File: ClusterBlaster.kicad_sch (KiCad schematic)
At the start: 12 parts, among them J1 Conn_01x04, U1 LM339, U2 L7805

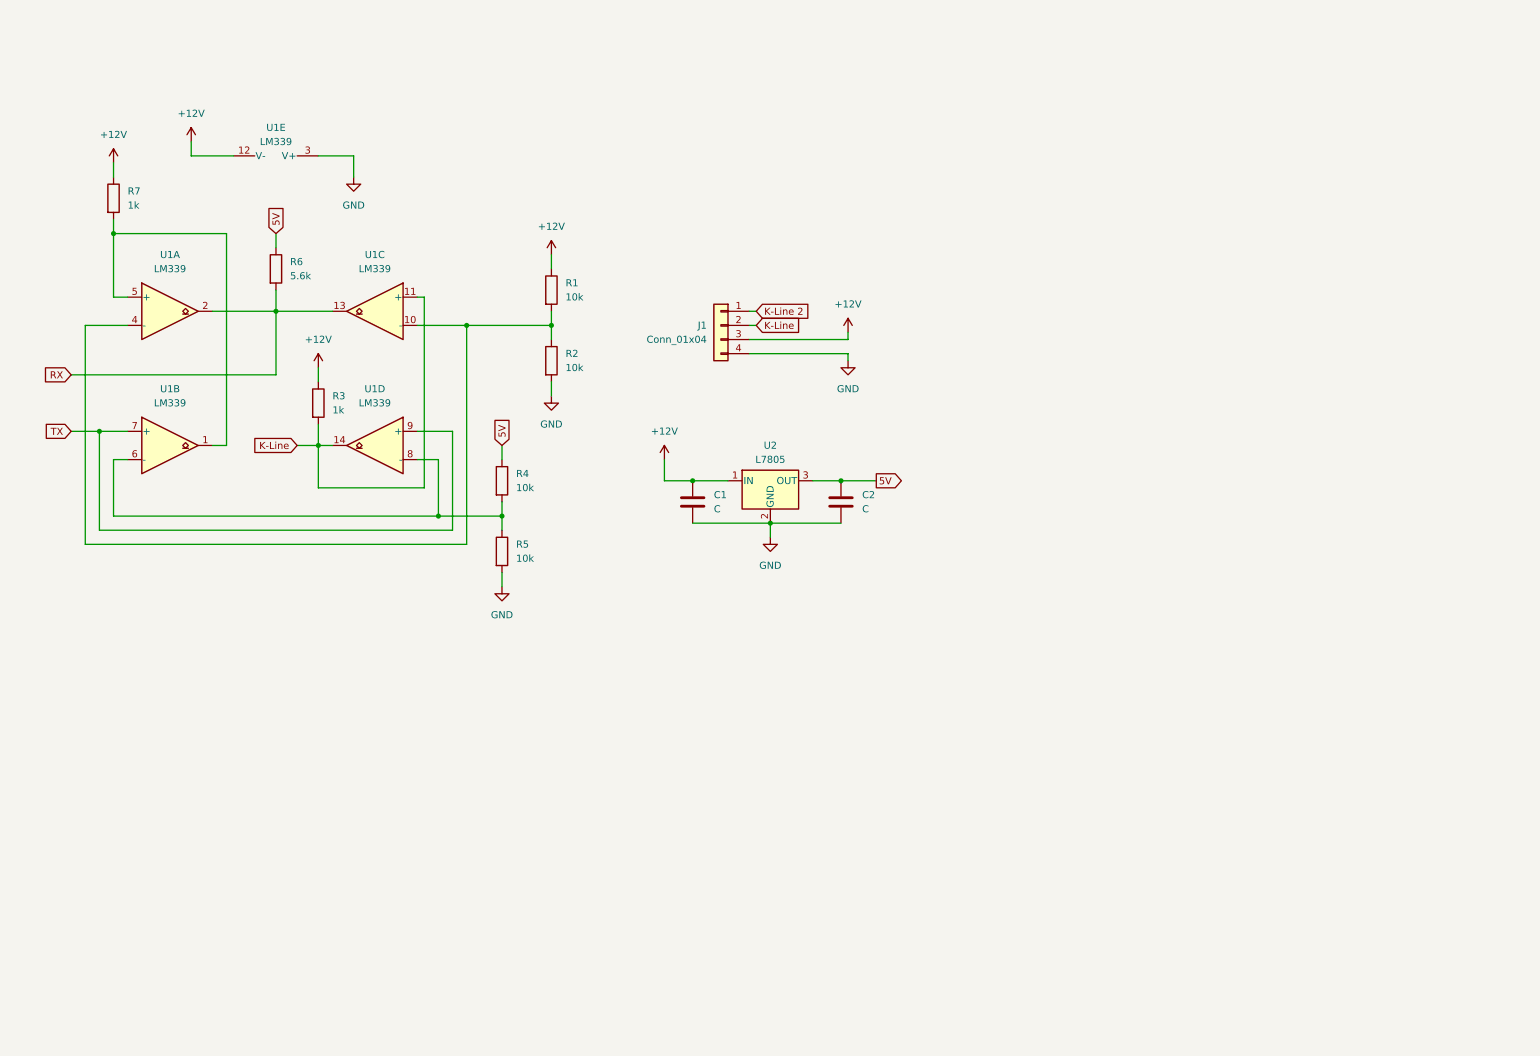
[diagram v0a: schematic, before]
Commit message: Added Arduino symbol and footprint
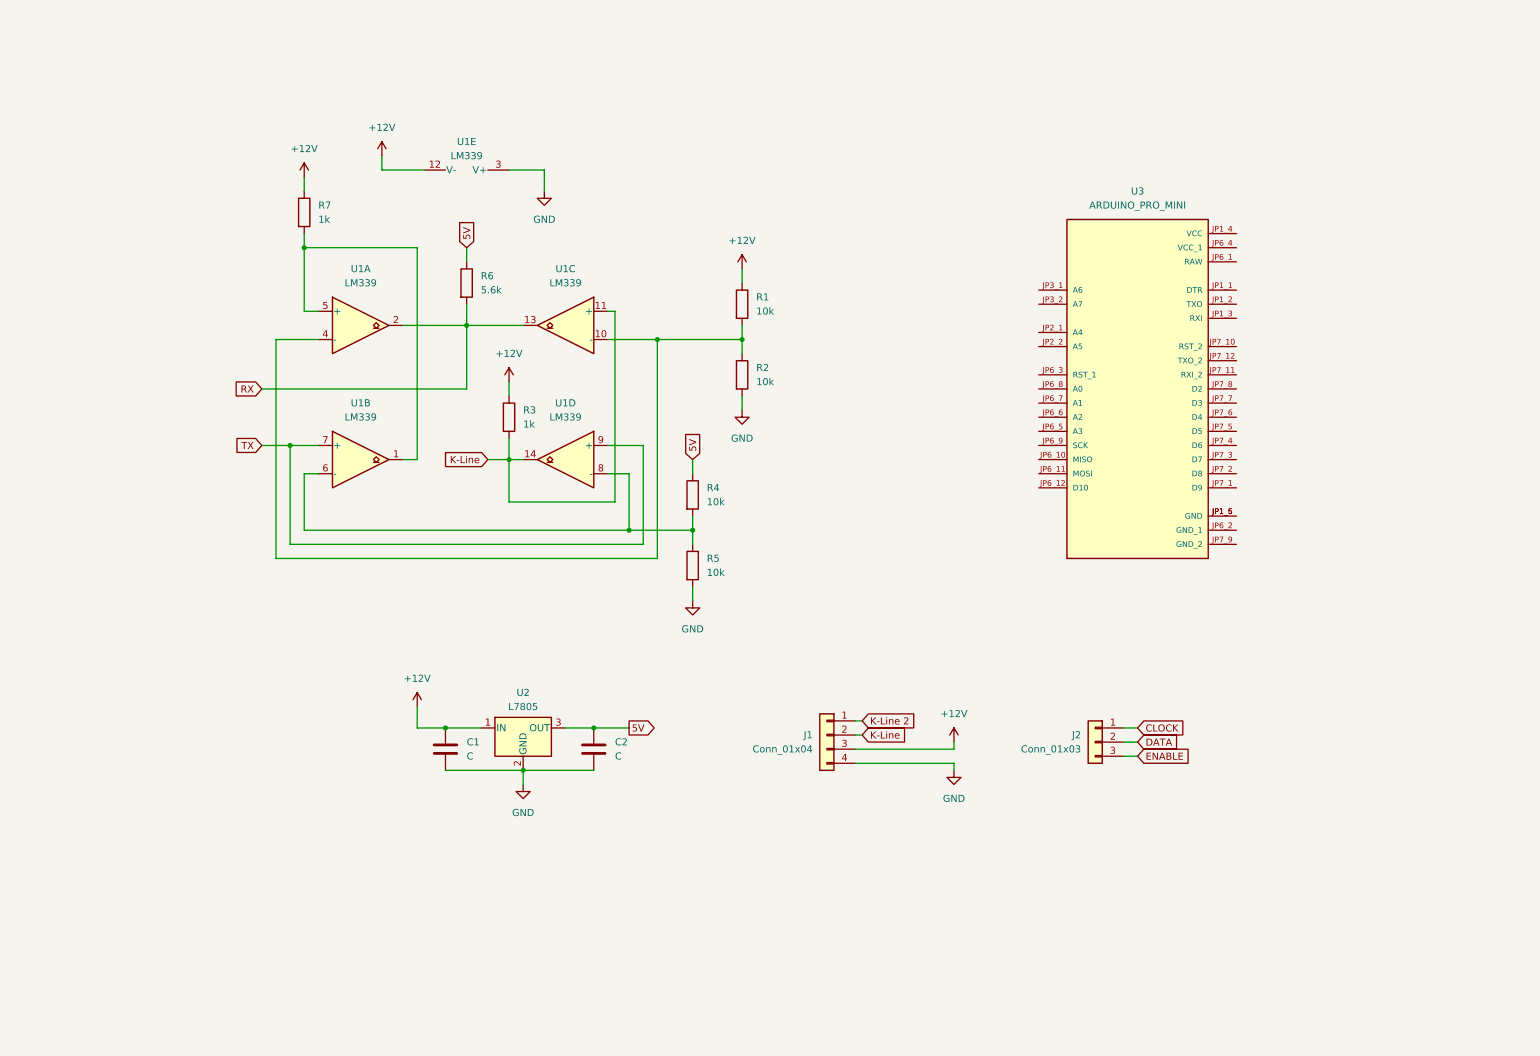
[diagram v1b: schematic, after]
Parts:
- added J2: Conn_01x03, Connector_JST:JST_EH_B3B-EH-A_1x03_P2.50mm_Vertical, symbol Connector_Generic:Conn_01x03
- added U3: ARDUINO_PRO_MINI, Pro_Mini:MODULE_ARDUINO_PRO_MINI, symbol ARDUINO_PRO_MINI:ARDUINO_PRO_MINI
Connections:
- new net: U3.JP1_5 (GND), U3.JP1_6 (GND)
- new net CLOCK: J2.1 (Pin_1)
- new net DATA: J2.2 (Pin_2)
- new net ENABLE: J2.3 (Pin_3)
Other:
- company: (none) -> Surdu Nicolae
- title: (none) -> ClusterBlaster
- moved on the sheet: C1, C2, J1, R1, R2, R3, R4, R5, R6, R7, U1A, U1B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

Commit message: Added all the components
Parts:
- added R10, R8, R9: 10k, Resistor_SMD:R_0805_2012Metric, symbol Device:R
- added SW1, SW2, SW3: SW_Push, Button_Switch_THT:SW_PUSH_6mm, symbol Switch:SW_Push
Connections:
- net 5V: now also U3.JP1_4 (VCC), U3.JP6_4 (VCC_1), SW1.2, SW2.2, SW3.2
- net CLOCK: now also U3.JP7_6 (D4)
- net DATA: now also U3.JP7_5 (D5)
- net ENABLE: now also U3.JP7_4 (D6)
- net GND: now also U3.JP1_5 (GND), U3.JP1_6 (GND), U3.JP6_2 (GND_1), U3.JP7_9 (GND_2), R10.1, R8.1, R9.1
- net RX: now also U3.JP7_8 (D2)
- net TX: now also U3.JP7_7 (D3)
- net BTN-UP: now reaches U3.JP7_1 (D9)
- net BTN-UP: now also R8.2, SW1.1
- net BTN-DOWN: now reaches U3.JP7_2 (D8)
- net BTN-DOWN: now also R9.2, SW2.1
- net BTN-ENTER: now reaches U3.JP7_3 (D7)
- net BTN-ENTER: now also R10.2, SW3.1
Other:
- moved on the sheet: C1, C2, J1, J2, U2

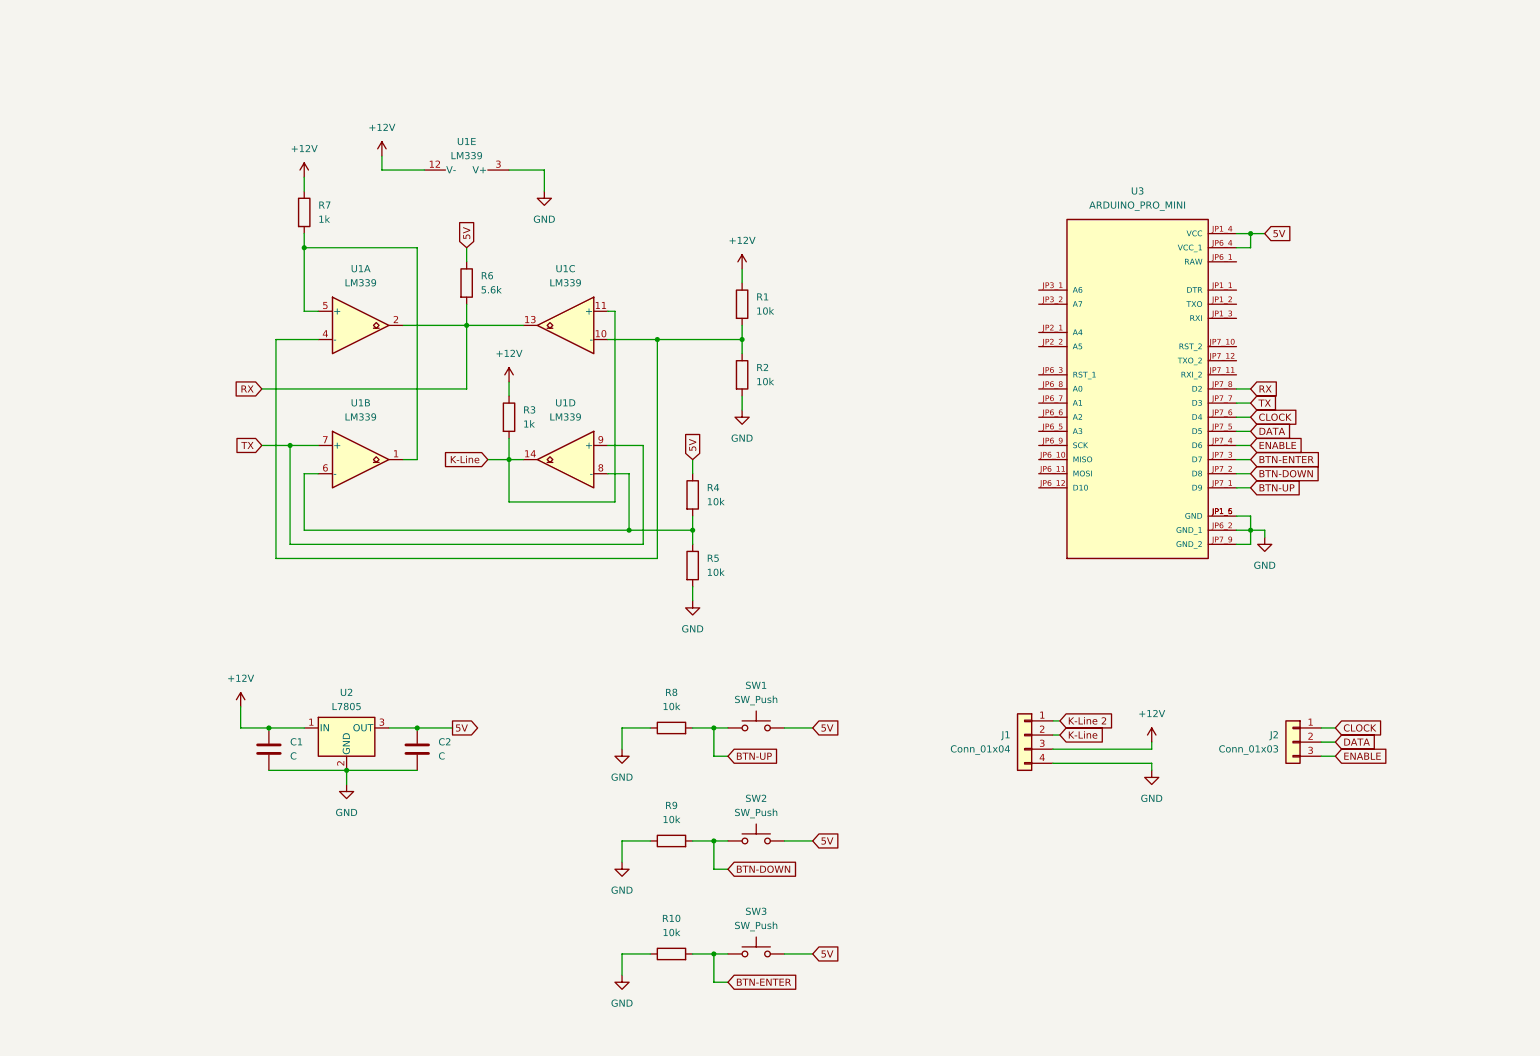
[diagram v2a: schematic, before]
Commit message: Started work on PCB layout
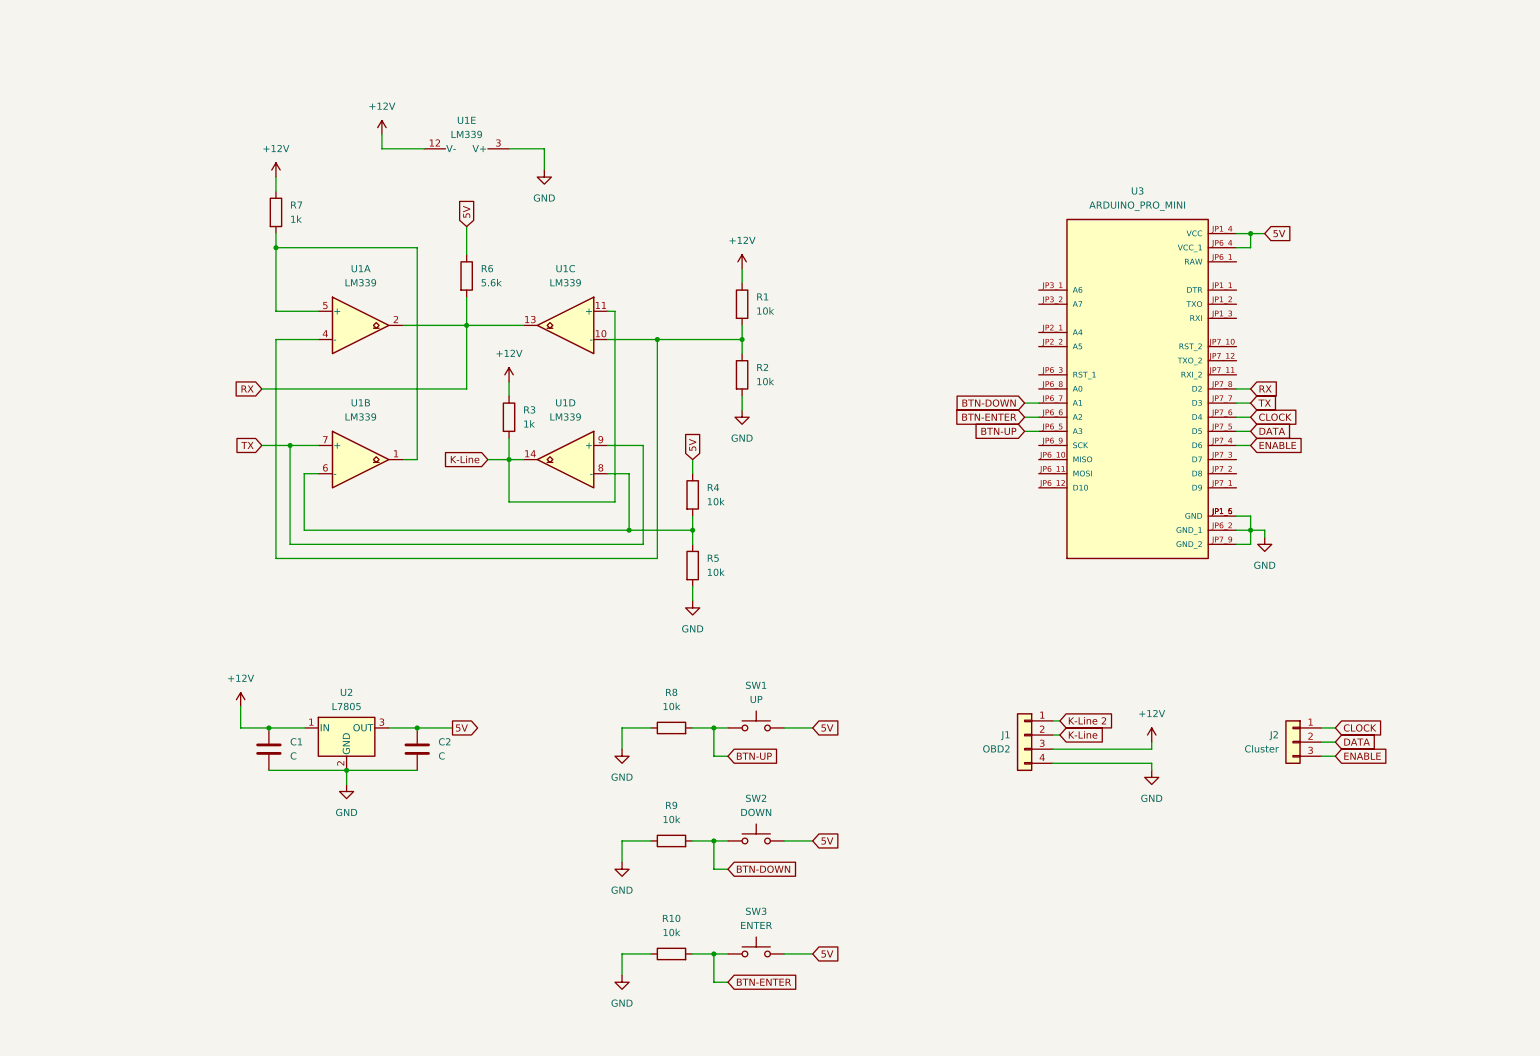
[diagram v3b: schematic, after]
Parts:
- J1: value Conn_01x04 -> OBD2
- J2: value Conn_01x03 -> Cluster
- SW1: value SW_Push -> UP
- SW2: value SW_Push -> DOWN
- SW3: value SW_Push -> ENTER
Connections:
- net BTN-DOWN: now also U3.JP6_7 (A1); no longer U3.JP7_2 (D8)
- net BTN-ENTER: now also U3.JP6_6 (A2); no longer U3.JP7_3 (D7)
- net BTN-UP: now also U3.JP6_5 (A3); no longer U3.JP7_1 (D9)
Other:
- moved on the sheet: R6, R7, U1E

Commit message: Switched Arduino to SMD sockets
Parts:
- U3: footprint Pro_Mini:MODULE_ARDUINO_PRO_MINI -> Arduino Pro Mini:PinSocket_1x12_P2.54mm_Vertical_SMD_Pin1Right
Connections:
- net 5V: no longer U3.JP1_4 (VCC)
- net GND: no longer U3.JP1_5 (GND), U3.JP1_6 (GND)
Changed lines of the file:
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@@
   (junction (at 72.39 148.59) (diameter 0) (color 0 0 0 0)
   )
-  (junction (at 234.95 52.07) (diameter 0) (color 0 0 0 0)
-  )
   (junction (at 62.23 90.17) (diameter 0) (color 0 0 0 0)
   )
@@
     (stroke (width 0) (type default))
   )
-  (wire (pts (xy 232.41 102.87) (xy 234.95 102.87))
-    (stroke (width 0) (type default))
-  )
   (wire (pts (xy 119.38 95.25) (xy 123.19 95.25))
     (stroke (width 0) (type default))
@@
     (stroke (width 0) (type default))
   )
-  (wire (pts (xy 234.95 52.07) (xy 234.95 54.61))
-    (stroke (width 0) (type default))
-  )
   (wire (pts (xy 247.65 143.51) (xy 250.19 143.51))
     (stroke (width 0) (type default))
@@
     (stroke (width 0) (type default))
   )
-  (wire (pts (xy 234.95 52.07) (xy 237.49 52.07))
-    (stroke (width 0) (type default))
-  )
   (wire (pts (xy 93.98 63.5) (xy 93.98 68.58))
     (stroke (width 0) (type default))
@@
     (stroke (width 0) (type default))
   )
-  (wire (pts (xy 232.41 52.07) (xy 234.95 52.07))
-    (stroke (width 0) (type default))
-  )
   (wire (pts (xy 138.43 161.29) (xy 138.43 166.37))
     (stroke (width 0) (type default))
@@
   )
   (wire (pts (xy 119.38 90.17) (xy 125.73 90.17))
-    (stroke (width 0) (type default))
-  )
-  (wire (pts (xy 234.95 105.41) (xy 234.95 102.87))
     (stroke (width 0) (type default))
   )
@@
     )
   )
-  (global_label "5V" (shape input) (at 237.49 52.07 0) (fields_autoplaced)
-    (effects (font (size 1.27 1.27)) (justify left))
-    (property "Intersheetrefs" "${INTERSHEET_REFS}" (at 242.7733 52.07 0)
+  (global_label "5V" (shape input) (at 234.95 54.61 0) (fields_autoplaced)
+    (effects (font (size 1.27 1.27)) (justify left))
+    (property "Intersheetrefs" "${INTERSHEET_REFS}" (at 240.2333 54.61 0)
       (effects (font (size 1.27 1.27)) (justify left) hide)
     )
@@
       (effects (font (size 1.27 1.27)))
     )
-    (property "Footprint" "Pro_Mini:MODULE_ARDUINO_PRO_MINI" (at 214.63 80.01 0)
+    (property "Footprint" "Arduino Pro Mini:PinSocket_1x12_P2.54mm_Vertical_SMD_Pin1Right" (at 214.63 80.01 0)
       (effects (font (size 1.27 1.27)) (justify bottom) hide)
     )
@@
       (effects (font (size 1.27 1.27)) (justify bottom) hide)
     )
-    (pin "JP1_1")
-    (pin "JP1_2")
-    (pin "JP1_3")
-    (pin "JP1_4")
-    (pin "JP1_5")
-    (pin "JP1_6")
-    (pin "JP2_1")
-    (pin "JP2_2")
-    (pin "JP3_1")
-    (pin "JP3_2")
     (pin "JP6_1")
     (pin "JP6_10")

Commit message: Routed PCB
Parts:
- removed J1: OBD2, Connector_JST:JST_EH_B4B-EH-A_1x04_P2.50mm_Vertical, symbol Connector_Generic:Conn_01x04
- added J1: OBD2, Connector_JST:JST_XH_B3B-XH-A_1x03_P2.50mm_Vertical, symbol Connector_Generic:Conn_01x03
- J2: value Cluster -> Cluster Display; footprint Connector_JST:JST_EH_B3B-EH-A_1x03_P2.50mm_Vertical -> Connector_JST:JST_XH_B3B-XH-A_1x03_P2.50mm_Vertical
- U3: footprint Arduino Pro Mini:PinSocket_1x12_P2.54mm_Vertical_SMD_Pin1Right -> Arduino Pro Mini:SMD
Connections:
- net +12V: now also J1.2 (Pin_2)
- net GND: now also J1.3 (Pin_3)
- net K-Line: now also J1.1 (Pin_1)
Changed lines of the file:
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@@
-    (stroke (width 0) (type default))
-  )
-  (wire (pts (xy 199.39 139.7) (xy 200.66 139.7))
     (stroke (width 0) (type default))
   )
@@
     (property "Intersheetrefs" "${INTERSHEET_REFS}" (at 51.6853 80.01 0)
       (effects (font (size 1.27 1.27)) (justify right) hide)
-    )
-  )
-  (global_label "K-Line 2" (shape input) (at 200.66 139.7 0) (fields_autoplaced)
-    (effects (font (size 1.27 1.27)) (justify left))
-    (property "Intersheetrefs" "${INTERSHEET_REFS}" (at 212.5352 139.7 0)
-      (effects (font (size 1.27 1.27)) (justify left) hide)
     )
   )
@@
       (effects (font (size 1.27 1.27)) (justify left))
     )
-    (property "Value" "Cluster" (at 240.03 144.78 0)
-      (effects (font (size 1.27 1.27)) (justify left))
-    )
-    (property "Footprint" "Connector_JST:JST_EH_B3B-EH-A_1x03_P2.50mm_Vertical" (at 242.57 143.51 0)
+    (property "Value" "Cluster Display" (at 240.03 144.78 0)
+      (effects (font (size 1.27 1.27)) (justify left))
+    )
+    (property "Footprint" "Connector_JST:JST_XH_B3B-XH-A_1x03_P2.50mm_Vertical" (at 242.57 143.51 0)
       (effects (font (size 1.27 1.27)) hide)
     )
@@
       (effects (font (size 1.27 1.27)))
     )
-    (property "Footprint" "Arduino Pro Mini:PinSocket_1x12_P2.54mm_Vertical_SMD_Pin1Right" (at 214.63 80.01 0)
+    (property "Footprint" "Arduino Pro Mini:SMD" (at 214.63 80.01 0)
       (effects (font (size 1.27 1.27)) (justify bottom) hide)
     )
@@
     )
   )
-  (symbol (lib_id "Connector_Generic:Conn_01x04") (at 194.31 142.24 0) (mirror y) (unit 1)
-    (in_bom yes) (on_board yes) (dnp no)
-    (property "Reference" "J1" (at 191.77 142.24 0)
-      (effects (font (size 1.27 1.27)) (justify left))
-    )
-    (property "Value" "OBD2" (at 191.77 144.78 0)
-      (effects (font (size 1.27 1.27)) (justify left))
-    )
-    (property "Footprint" "Connector_JST:JST_EH_B4B-EH-A_1x04_P2.50mm_Vertical" (at 194.31 142.24 0)
-      (effects (font (size 1.27 1.27)) hide)
-    )
-    (property "Datasheet" "~" (at 194.31 142.24 0)
-      (effects (font (size 1.27 1.27)) hide)
-    )
-    (pin "1")
-    (pin "2")
-    (pin "3")
-    (pin "4")
-    (instances
-      (project "ClusterBlaster"
-        (path "/f0c30adf-63bc-461a-bbad-df5b5e088925"
-          (reference "J1") (unit 1)
-        )
-      )
-    )
-  )
   (symbol (lib_id "power:+12V") (at 101.6 78.74 0) (unit 1)
     (in_bom yes) (on_board yes) (dnp no) (fields_autoplaced)
@@
         )
       )
+    )
+  )
+  (symbol (lib_id "Connector_Generic:Conn_01x03") (at 194.31 144.78 0) (mirror y) (unit 1)
+    (in_bom yes) (on_board yes) (dnp no)
+    (property "Reference" "J1" (at 191.77 143.51 0)
+      (effects (font (size 1.27 1.27)) (justify left))
+    )
+    (property "Value" "OBD2" (at 191.77 146.05 0)
+      (effects (font (size 1.27 1.27)) (justify left))
+    )
+    (property "Footprint" "Connector_JST:JST_XH_B3B-XH-A_1x03_P2.50mm_Vertical" (at 194.31 144.78 0)
+      (effects (font (size 1.27 1.27)) hide)
+    )
+    (property "Datasheet" "~" (at 194.31 144.78 0)
+      (effects (font (size 1.27 1.27)) hide)
+    )
+    (pin "1")
+    (pin "2")
+    (pin "3")
+    (instances
+      (project "ClusterBlaster"
+        (path "/f0c30adf-63bc-461a-bbad-df5b5e088925"
+          (reference "J1") (unit 1)
+        )
+      )
